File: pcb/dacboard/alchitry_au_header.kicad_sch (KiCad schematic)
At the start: 10 parts, among them J14 Conn_01x14, J15 Conn_01x14, J17 Conn_01x14, J18 Conn_01x14, J19 Conn_01x14, J20 Conn_01x14, J21 Conn_01x14, J22 Conn_01x06, J4 Conn_01x14, J6 Conn_01x14

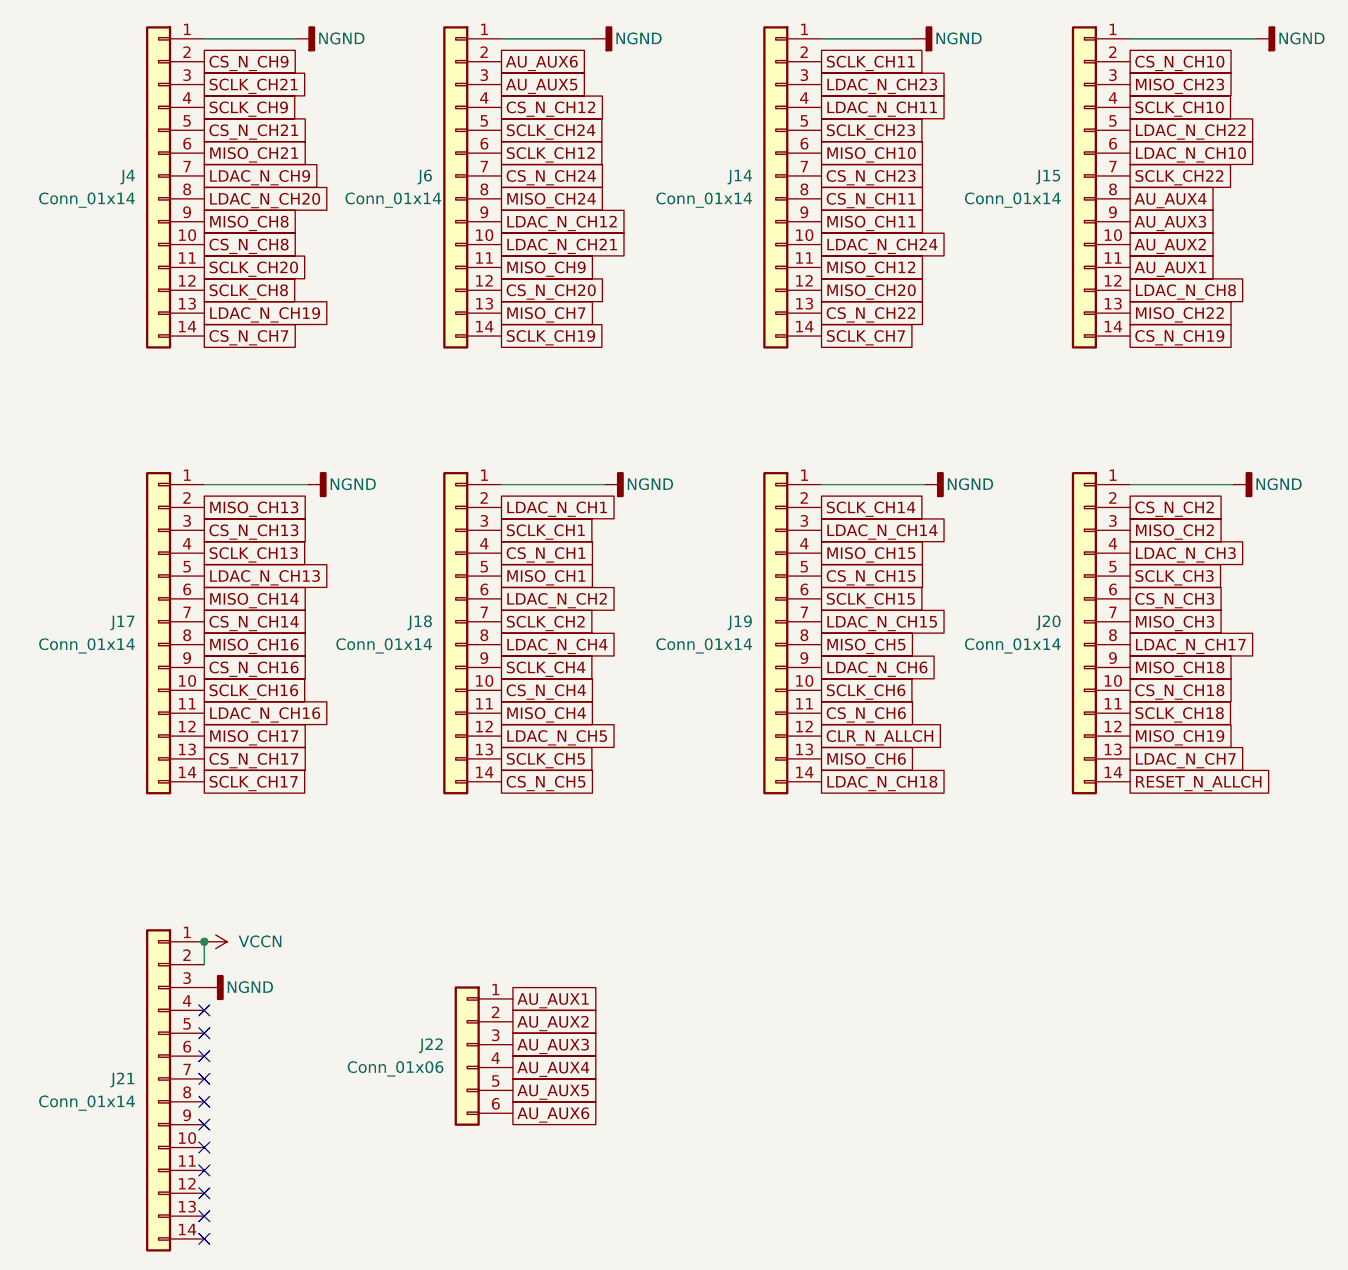
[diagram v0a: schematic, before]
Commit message: fixed mosi miso flip in inner section
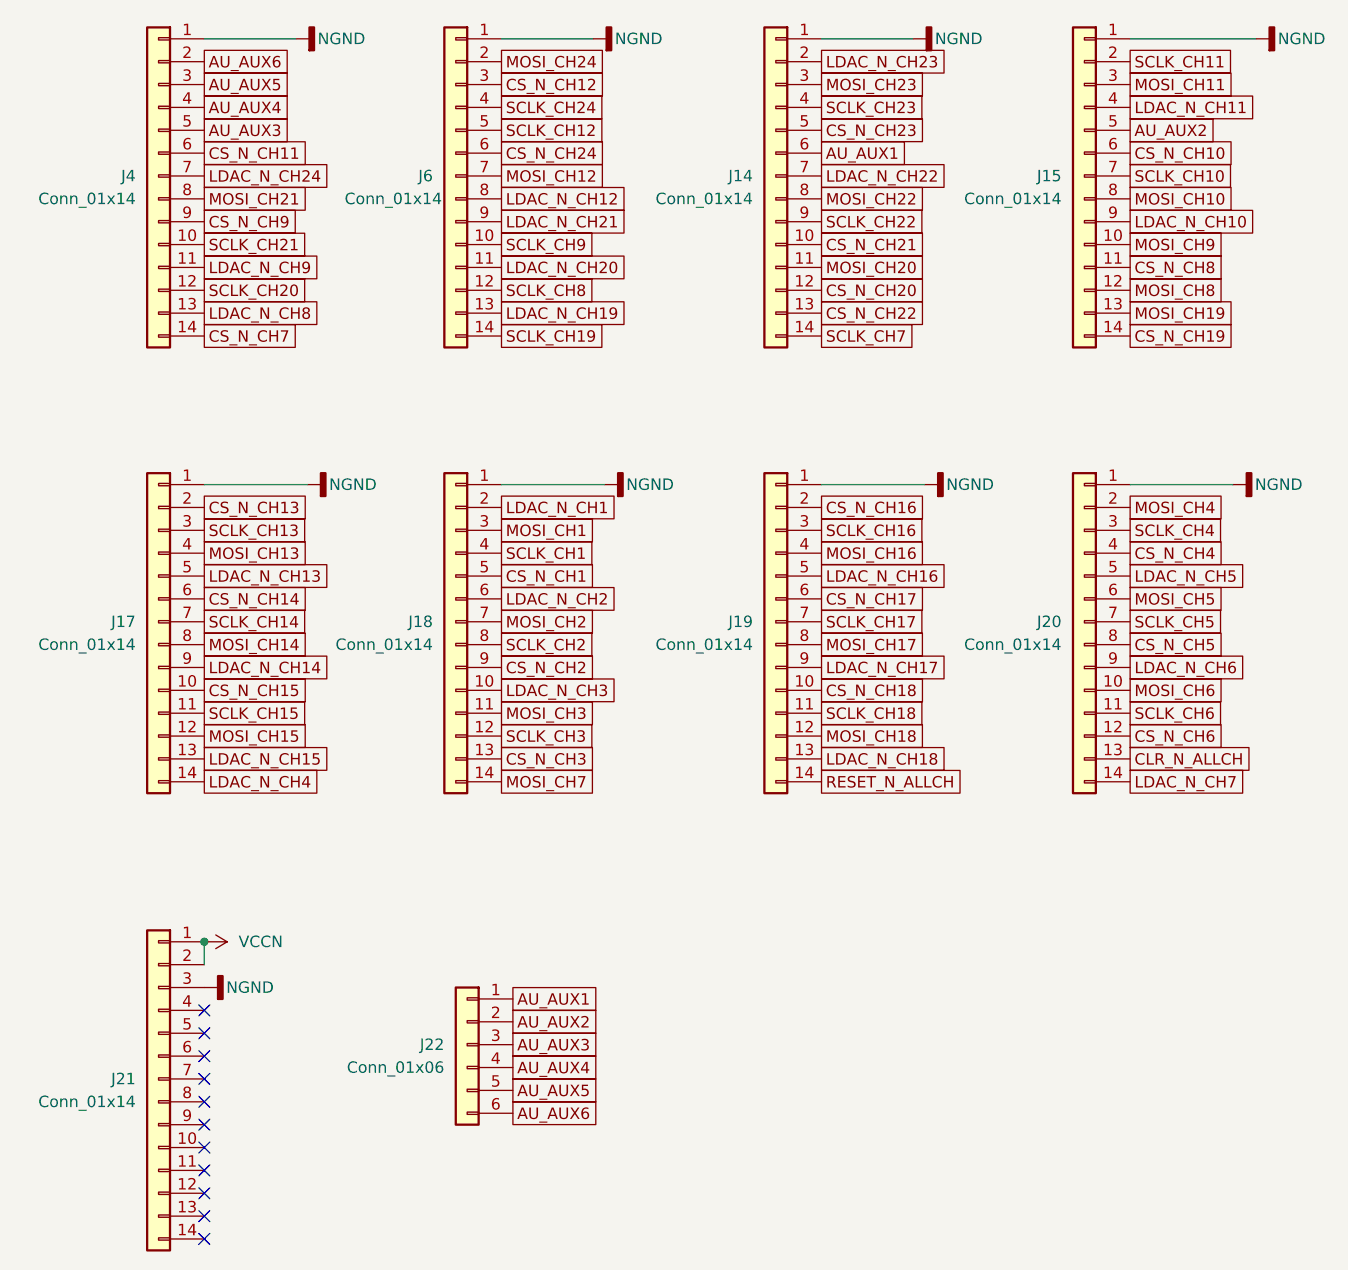
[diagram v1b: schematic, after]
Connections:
- net MISO_CH1 is gone; now on net CS_N_CH1: J18.5 (Pin_5)
- net MISO_CH10 is gone; now on net AU_AUX1: J14.6 (Pin_6)
- net MISO_CH11 is gone; now on net SCLK_CH22: J14.9 (Pin_9)
- net MISO_CH13 is gone; now on net CS_N_CH13: J17.2 (Pin_2)
- net MISO_CH14 is gone; now on net CS_N_CH14: J17.6 (Pin_6)
- net MISO_CH18 is gone; now on net LDAC_N_CH6: J20.9 (Pin_9)
- net MISO_CH19 is gone; now on net CS_N_CH6: J20.12 (Pin_12)
- net MISO_CH2 is gone; now on net SCLK_CH4: J20.3 (Pin_3)
- net MISO_CH20 is gone; now on net CS_N_CH20: J14.12 (Pin_12)
- net MISO_CH21 is gone; now on net CS_N_CH11: J4.6 (Pin_6)
- net MISO_CH24 is gone; now on net LDAC_N_CH12: J6.8 (Pin_8)
- net MISO_CH3 is gone; now on net SCLK_CH5: J20.7 (Pin_7)
- net MISO_CH6 is gone; now on net LDAC_N_CH18: J19.13 (Pin_13)
- net MISO_CH7 is gone; now on net LDAC_N_CH19: J6.13 (Pin_13)
- net MISO_CH8 is gone; now on net CS_N_CH9: J4.9 (Pin_9)
- net MISO_CH9 is gone; now on net LDAC_N_CH20: J6.11 (Pin_11)
- net AU_AUX1: no longer J15.11 (Pin_11)
- net AU_AUX2: now also J15.5 (Pin_5); no longer J15.10 (Pin_10)
- net AU_AUX3: now also J4.5 (Pin_5); no longer J15.9 (Pin_9)
- net AU_AUX4: now also J4.4 (Pin_4); no longer J15.8 (Pin_8)
- net AU_AUX5: now also J4.3 (Pin_3); no longer J6.3 (Pin_3)
- net AU_AUX6: now also J4.2 (Pin_2); no longer J6.2 (Pin_2)
- net CLR_N_ALLCH: now also J20.13 (Pin_13); no longer J19.12 (Pin_12)
- net CS_N_CH1: no longer J18.4 (Pin_4)
- net CS_N_CH10: now also J15.6 (Pin_6); no longer J15.2 (Pin_2)
- net CS_N_CH11: no longer J14.8 (Pin_8)
- net CS_N_CH12: now also J6.3 (Pin_3); no longer J6.4 (Pin_4)
- net CS_N_CH13: no longer J17.3 (Pin_3)
- net CS_N_CH14: no longer J17.7 (Pin_7)
- net CS_N_CH15: now also J17.10 (Pin_10); no longer J19.5 (Pin_5)
- net CS_N_CH16: now also J19.2 (Pin_2); no longer J17.9 (Pin_9)
- net CS_N_CH17: now also J19.6 (Pin_6); no longer J17.13 (Pin_13)
- net CS_N_CH18: now also J19.10 (Pin_10); no longer J20.10 (Pin_10)
- net CS_N_CH2: now also J18.9 (Pin_9); no longer J20.2 (Pin_2)
- net CS_N_CH20: no longer J6.12 (Pin_12)
- net CS_N_CH21: now also J14.10 (Pin_10); no longer J4.5 (Pin_5)
- net CS_N_CH23: now also J14.5 (Pin_5); no longer J14.7 (Pin_7)
- net CS_N_CH24: now also J6.6 (Pin_6); no longer J6.7 (Pin_7)
- net CS_N_CH3: now also J18.13 (Pin_13); no longer J20.6 (Pin_6)
- net CS_N_CH4: now also J20.4 (Pin_4); no longer J18.10 (Pin_10)
- net CS_N_CH5: now also J20.8 (Pin_8); no longer J18.14 (Pin_14)
- net CS_N_CH6: no longer J19.11 (Pin_11)
- net CS_N_CH8: now also J15.11 (Pin_11); no longer J4.10 (Pin_10)
- net CS_N_CH9: no longer J4.2 (Pin_2)
- net LDAC_N_CH10: now also J15.9 (Pin_9); no longer J15.6 (Pin_6)
- net LDAC_N_CH11: now also J15.4 (Pin_4); no longer J14.4 (Pin_4)
- net LDAC_N_CH12: no longer J6.9 (Pin_9)
- net LDAC_N_CH14: now also J17.9 (Pin_9); no longer J19.3 (Pin_3)
- net LDAC_N_CH15: now also J17.13 (Pin_13); no longer J19.7 (Pin_7)
- net LDAC_N_CH16: now also J19.5 (Pin_5); no longer J17.11 (Pin_11)
- net LDAC_N_CH17: now also J19.9 (Pin_9); no longer J20.8 (Pin_8)
- net LDAC_N_CH18: no longer J19.14 (Pin_14)
- net LDAC_N_CH19: no longer J4.13 (Pin_13)
- net LDAC_N_CH20: no longer J4.8 (Pin_8)
- net LDAC_N_CH21: now also J6.9 (Pin_9); no longer J6.10 (Pin_10)
- net LDAC_N_CH22: now also J14.7 (Pin_7); no longer J15.5 (Pin_5)
- net LDAC_N_CH23: now also J14.2 (Pin_2); no longer J14.3 (Pin_3)
- net LDAC_N_CH24: now also J4.7 (Pin_7); no longer J14.10 (Pin_10)
- net LDAC_N_CH3: now also J18.10 (Pin_10); no longer J20.4 (Pin_4)
- net LDAC_N_CH4: now also J17.14 (Pin_14); no longer J18.8 (Pin_8)
- net LDAC_N_CH5: now also J20.5 (Pin_5); no longer J18.12 (Pin_12)
- net LDAC_N_CH6: no longer J19.9 (Pin_9)
- net LDAC_N_CH7: now also J20.14 (Pin_14); no longer J20.13 (Pin_13)
- net LDAC_N_CH8: now also J4.13 (Pin_13); no longer J15.12 (Pin_12)
- net LDAC_N_CH9: now also J4.11 (Pin_11); no longer J4.7 (Pin_7)
- net RESET_N_ALLCH: now also J19.14 (Pin_14); no longer J20.14 (Pin_14)
- net SCLK_CH1: now also J18.4 (Pin_4); no longer J18.3 (Pin_3)
- net SCLK_CH10: now also J15.7 (Pin_7); no longer J15.4 (Pin_4)
- net SCLK_CH11: now also J15.2 (Pin_2); no longer J14.2 (Pin_2)
- net SCLK_CH12: now also J6.5 (Pin_5); no longer J6.6 (Pin_6)
- net SCLK_CH13: now also J17.3 (Pin_3); no longer J17.4 (Pin_4)
- net SCLK_CH14: now also J17.7 (Pin_7); no longer J19.2 (Pin_2)
- net SCLK_CH15: now also J17.11 (Pin_11); no longer J19.6 (Pin_6)
- net SCLK_CH16: now also J19.3 (Pin_3); no longer J17.10 (Pin_10)
- net SCLK_CH17: now also J19.7 (Pin_7); no longer J17.14 (Pin_14)
- net SCLK_CH18: now also J19.11 (Pin_11); no longer J20.11 (Pin_11)
- net SCLK_CH2: now also J18.8 (Pin_8); no longer J18.7 (Pin_7)
- net SCLK_CH20: now also J4.12 (Pin_12); no longer J4.11 (Pin_11)
- net SCLK_CH21: now also J4.10 (Pin_10); no longer J4.3 (Pin_3)
- net SCLK_CH22: no longer J15.7 (Pin_7)
- net SCLK_CH23: now also J14.4 (Pin_4); no longer J14.5 (Pin_5)
- net SCLK_CH24: now also J6.4 (Pin_4); no longer J6.5 (Pin_5)
- net SCLK_CH3: now also J18.12 (Pin_12); no longer J20.5 (Pin_5)
- net SCLK_CH4: no longer J18.9 (Pin_9)
- net SCLK_CH5: no longer J18.13 (Pin_13)
- net SCLK_CH6: now also J20.11 (Pin_11); no longer J19.10 (Pin_10)
- net SCLK_CH8: now also J6.12 (Pin_12); no longer J4.12 (Pin_12)
- net SCLK_CH9: now also J6.10 (Pin_10); no longer J4.4 (Pin_4)
- net MISO_CH12 renamed MOSI_CH20
- net MISO_CH15 renamed MOSI_CH16
- net MISO_CH16 renamed MOSI_CH14
- net MISO_CH17 renamed MOSI_CH15
- net MISO_CH22 renamed MOSI_CH19
- net MISO_CH23 renamed MOSI_CH11
- net MISO_CH4 renamed MOSI_CH3
- net MISO_CH5 renamed MOSI_CH17
- new net MOSI_CH1: J18.3 (Pin_3)
- new net MOSI_CH10: J15.8 (Pin_8)
- new net MOSI_CH12: J6.7 (Pin_7)
- new net MOSI_CH13: J17.4 (Pin_4)
- new net MOSI_CH18: J19.12 (Pin_12)
- new net MOSI_CH2: J18.7 (Pin_7)
- new net MOSI_CH21: J4.8 (Pin_8)
- new net MOSI_CH22: J14.8 (Pin_8)
- new net MOSI_CH23: J14.3 (Pin_3)
- new net MOSI_CH24: J6.2 (Pin_2)
- new net MOSI_CH4: J20.2 (Pin_2)
- new net MOSI_CH5: J20.6 (Pin_6)
- new net MOSI_CH6: J20.10 (Pin_10)
- new net MOSI_CH7: J18.14 (Pin_14)
- new net MOSI_CH8: J15.12 (Pin_12)
- new net MOSI_CH9: J15.10 (Pin_10)
